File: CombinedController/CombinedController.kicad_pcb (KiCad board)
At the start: 2 copper layers, 2 parts

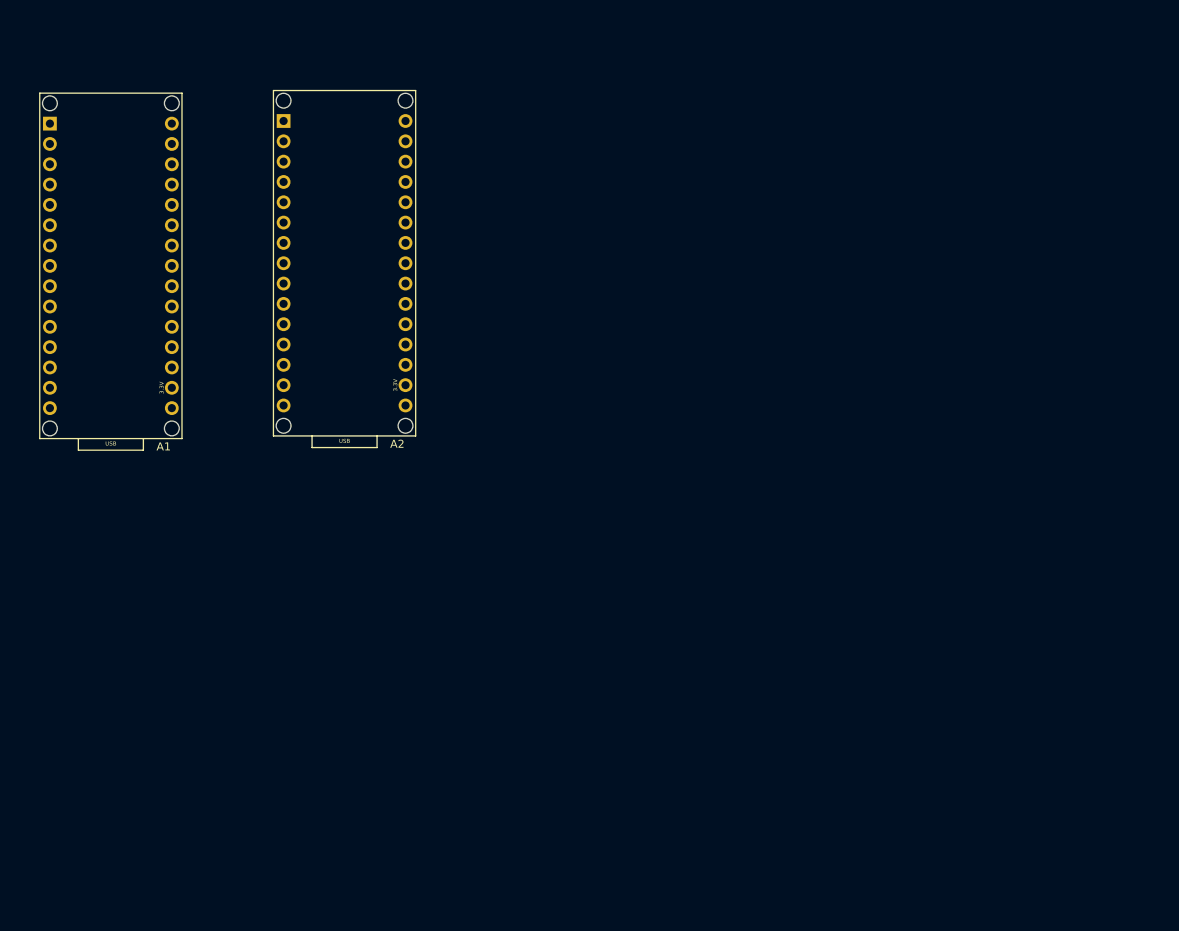
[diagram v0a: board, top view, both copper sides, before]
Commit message: Add MC33886 Footprint and fix schematics
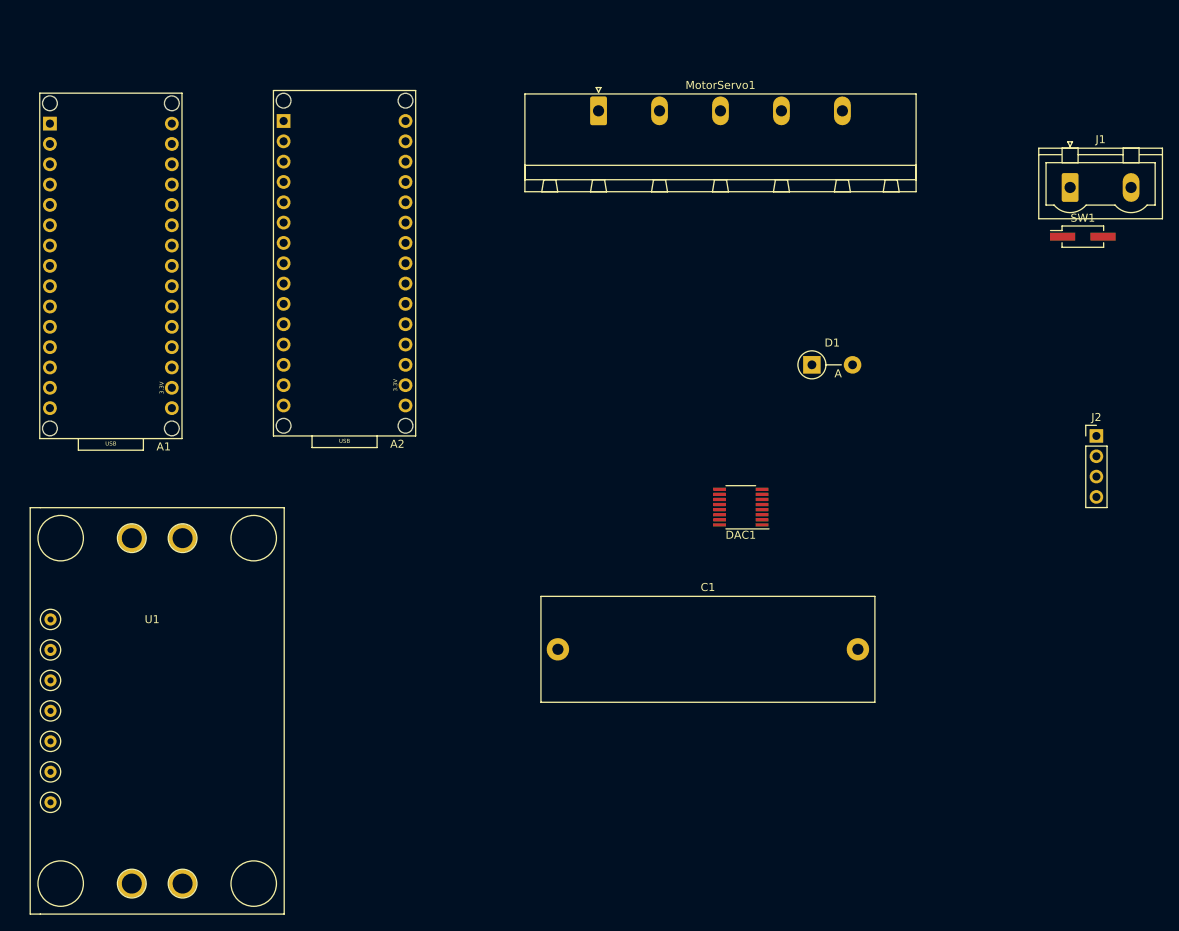
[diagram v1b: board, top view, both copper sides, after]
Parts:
- added C1: C, Capacitor_THT:C_Rect_L41.5mm_W13.0mm_P37.50mm_MKS4, F.Cu at (179.1, 137.2)
- added D1: DIODE, Diode_THT:D_DO-41_SOD81_P5.08mm_Vertical_AnodeUp, F.Cu at (210.8, 101.6)
- added DAC1: MAX5259, Package_SO:QSOP-16_3.9x4.9mm_P0.635mm, F.Cu at (201.9, 119.4)
- added J1: Conn_01x02_Male, Connector_Phoenix_GMSTB:PhoenixContact_GMSTBVA_2,5_2-G-7,62_1x02_P7.62mm_Vertical, F.Cu at (243.1, 79.4)
- added J2: APA102C, Connector_PinHeader_2.54mm:PinHeader_1x04_P2.54mm_Vertical, F.Cu at (246.4, 110.5)
- added MotorServo1: Conn_01x05_Female, Connector_Phoenix_GMSTB:PhoenixContact_GMSTB_2,5_5-GF-7,62_1x05_P7.62mm_Horizontal_ThreadedFlange, F.Cu at (184.2, 69.8)
- added SW1: SW_Push, Connector_PinHeader_2.54mm:PinHeader_2x01_P2.54mm_Vertical_SMD, F.Cu at (244.7, 85.6)
- added U1: MC33886, Arduino:MC33886, F.Cu at (128.3, 132.2)

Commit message: added tle started pcb layouting
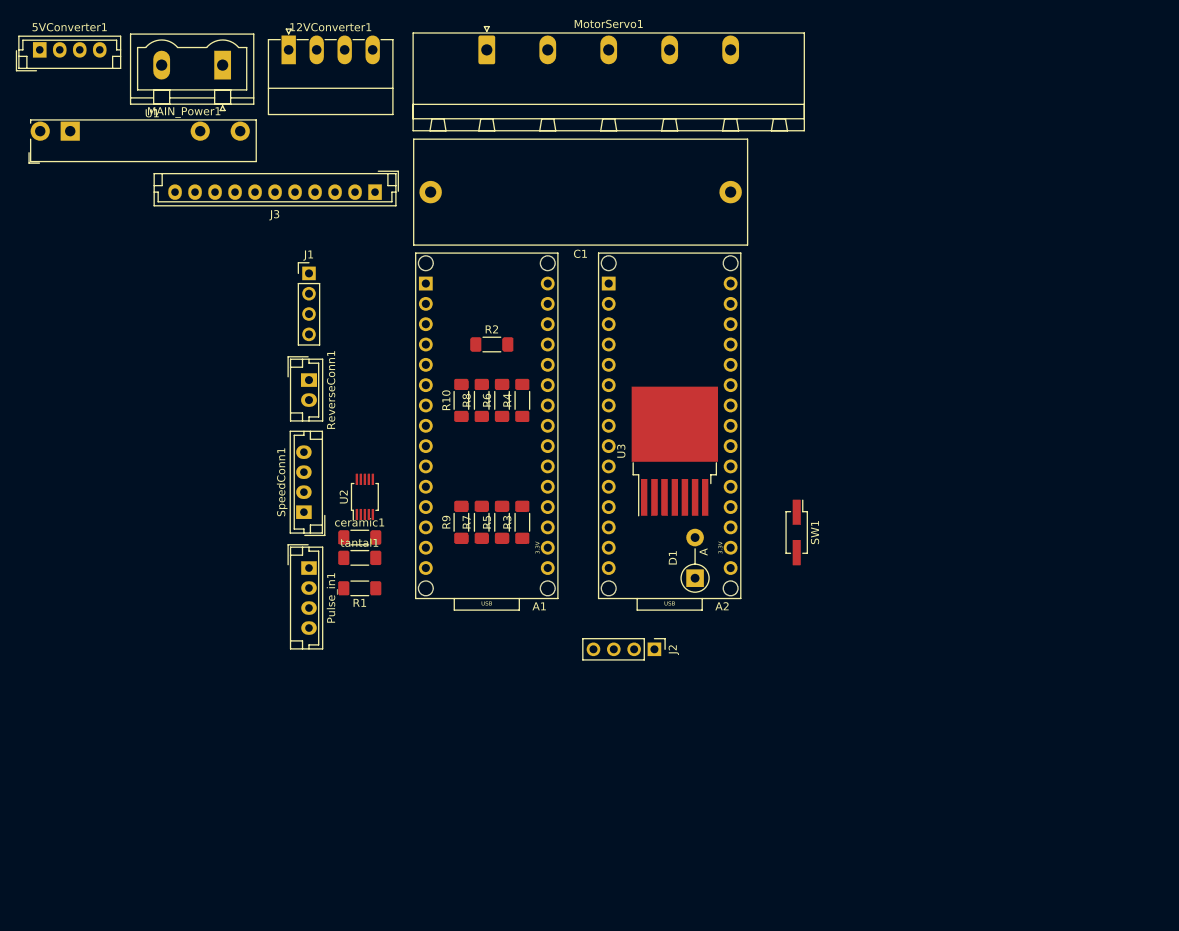
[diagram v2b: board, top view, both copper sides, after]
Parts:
- removed DAC1: MAX5259, Package_SO:QSOP-16_3.9x4.9mm_P0.635mm
- added 12VConverter1: Conn_01x04_Male, Connector_Phoenix_MC:PhoenixContact_MC_1,5_4-G-3.5_1x04_P3.50mm_Horizontal, F.Cu at (145.4, 62.2)
- added 5VConverter1: Conn_01x04_Male, Connector_JST:JST_EH_B04B-EH-A_1x04_P2.50mm_Vertical, F.Cu at (114.3, 62.2)
- added J3: Conn_01x11_Male, Connector_JST:JST_EH_B11B-EH-A_1x11_P2.50mm_Vertical, F.Cu at (156.2, 80.0)
- added MAIN_Power1: Conn_01x02_Male, Connector_Phoenix_GMSTB:PhoenixContact_GMSTBVA_2,5_2-G-7,62_1x02_P7.62mm_Vertical, F.Cu at (137.2, 64.1)
- added Pulse_in1: Conn_01x04_Male, Connector_JST:JST_EH_B04B-EH-A_1x04_P2.50mm_Vertical, F.Cu at (148.0, 127.0)
- added R1: 10kOhm, Resistor_SMD:R_1806_4516Metric, F.Cu at (154.3, 129.5)
- added R10: 1kohm, Resistor_SMD:R_1806_4516Metric, F.Cu at (167.0, 106.0)
- added R2: 10kOhm, Resistor_SMD:R_1806_4516Metric, F.Cu at (170.8, 99.1)
- added R3: R, Resistor_SMD:R_1806_4516Metric, F.Cu at (174.6, 121.3)
- added R4: R, Resistor_SMD:R_1806_4516Metric, F.Cu at (174.6, 106.0)
- added R5: R, Resistor_SMD:R_1806_4516Metric, F.Cu at (172.1, 121.3)
- added R6: R, Resistor_SMD:R_1806_4516Metric, F.Cu at (172.1, 106.0)
- added R7: R, Resistor_SMD:R_1806_4516Metric, F.Cu at (169.5, 121.3)
- added R8: R, Resistor_SMD:R_1806_4516Metric, F.Cu at (169.5, 106.0)
- added R9: 10kohm, Resistor_SMD:R_1806_4516Metric, F.Cu at (167.0, 121.3)
- added ReverseConn1: Conn_01x02_Male, Connector_JST:JST_EH_B02B-EH-A_1x02_P2.50mm_Vertical, F.Cu at (148.0, 103.5)
- added SpeedConn1: Conn_01x04_Male, Connector_JST:JST_EH_B04B-EH-A_1x04_P2.50mm_Vertical, F.Cu at (147.3, 120.0)
- added U2: MCP4728, Package_SO:MSOP-10_3x3mm_P0.5mm, F.Cu at (154.9, 118.1)
- added U3: TLE5205, Package_TO_SOT_SMD:TO-263-7_TabPin4, F.Cu at (193.7, 112.4)
- added ceramic1: 0.1uF, Capacitor_SMD:C_1806_4516Metric, F.Cu at (154.3, 123.2)
- added tantal1: 10uF, Capacitor_SMD:C_1806_4516Metric, F.Cu at (154.3, 125.7)
- J1: value Conn_01x02_Male -> APA102C; footprint Connector_Phoenix_GMSTB:PhoenixContact_GMSTBVA_2,5_2-G-7,62_1x02_P7.62mm_Vertical -> Connector_PinHeader_2.54mm:PinHeader_1x04_P2.54mm_Vertical
- U1: value MC33886 -> 34.81-8240; footprint Arduino:MC33886 -> OptoDevice:Finder_34.81
- moved J1 95.7 mm to (148.0, 90.2)
- moved J2 61.3 mm to (191.1, 137.2), turned to 270 degrees
- moved C1 61.1 mm to (200.7, 80.0), turned to 180 degrees
- moved U1 60.6 mm to (118.1, 72.4)
- moved SW1 51.4 mm to (208.9, 122.6), turned to 270 degrees
- moved A1 51.1 mm to (170.2, 130.8)
- moved A2 45.4 mm to (193.0, 130.8)
- moved D1 30.4 mm to (196.2, 128.3), turned to 90 degrees
- moved MotorServo1 15.9 mm to (170.2, 62.2)
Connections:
- A1 pad 3V3: (no net) -> Net-(A1-Pad3V3)
- A1 pad 5V: (no net) -> 5V_Main
- A1 pad A0: (no net) -> Net-(A1-PadA0)
- A1 pad A1: (no net) -> Net-(A1-PadA1)
- A1 pad A2: (no net) -> Net-(A1-PadA2)
- A1 pad A3: (no net) -> Net-(A1-PadA3)
- A1 pad A4: (no net) -> Net-(A1-PadA4)
- A1 pad A5: (no net) -> Net-(A1-PadA5)
- A1 pad A6: (no net) -> Net-(A1-PadA6)
- A1 pad A7: (no net) -> Net-(A1-PadA7)
- A1 pad AREF: (no net) -> Net-(A1-PadAREF)
- A1 pad D0: (no net) -> Net-(A1-PadD0)
- A1 pad D1: (no net) -> Net-(A1-PadD1)
- A1 pad D10: (no net) -> Net-(A1-PadD10)
- A1 pad D11: (no net) -> Net-(A1-PadD11)
- A1 pad D12: (no net) -> Net-(A1-PadD12)
- A1 pad D13: (no net) -> Net-(A1-PadD13)
- A1 pad D2: (no net) -> Net-(A1-PadD2)
- A1 pad D3: (no net) -> Net-(A1-PadD3)
- A1 pad D4: (no net) -> Mode
- A1 pad D5: (no net) -> Lenkung
- A1 pad D6: (no net) -> Throttle
- A1 pad D7: (no net) -> Net-(A1-PadD7)
- A1 pad D8: (no net) -> Net-(A1-PadD8)
- A1 pad D9: (no net) -> Net-(A1-PadD9)
- A1 pad GND1: (no net) -> GND
- A1 pad GND2: (no net) -> GND
- A1 pad RST1: (no net) -> Net-(A1-PadRST1)
- A1 pad RST2: (no net) -> Net-(A1-PadRST2)
- A1 pad VIN: (no net) -> Net-(A1-PadVIN)
- A2 pad 3V3: (no net) -> Net-(A2-Pad3V3)
- A2 pad 5V: (no net) -> 5V_2
- A2 pad A0: (no net) -> Net-(A2-PadA0)
- A2 pad A1: (no net) -> Net-(A2-PadA1)
- A2 pad A2: (no net) -> Net-(A2-PadA2)
- A2 pad A3: (no net) -> Net-(A2-PadA3)
- A2 pad A4: (no net) -> Net-(A2-PadA4)
- A2 pad A5: (no net) -> Net-(A2-PadA5)
- A2 pad A6: (no net) -> Net-(A2-PadA6)
- A2 pad A7: (no net) -> Net-(A2-PadA7)
- A2 pad AREF: (no net) -> Net-(A2-PadAREF)
- A2 pad D0: (no net) -> Net-(A2-PadD0)
- A2 pad D1: (no net) -> Net-(A2-PadD1)
- A2 pad D10: (no net) -> Net-(A2-PadD10)
- A2 pad D11: (no net) -> Net-(A2-PadD11)
- A2 pad D12: (no net) -> Lenkung
- A2 pad D13: (no net) -> Net-(A2-PadD13)
- A2 pad D2: (no net) -> Net-(A2-PadD2)
- A2 pad D3: (no net) -> Net-(A2-PadD3)
- A2 pad D4: (no net) -> Net-(A2-PadD4)
- A2 pad D5: (no net) -> Net-(A2-PadD5)
- A2 pad D6: (no net) -> Net-(A2-PadD6)
- A2 pad D7: (no net) -> Net-(A2-PadD7)
- A2 pad D8: (no net) -> Net-(A2-PadD8)
- A2 pad D9: (no net) -> Net-(A2-PadD9)
- A2 pad GND1: (no net) -> GND
- A2 pad GND2: (no net) -> GND
- A2 pad RST1: (no net) -> Net-(A2-PadRST1)
- A2 pad RST2: (no net) -> Net-(A2-PadRST2)
- A2 pad VIN: (no net) -> 12V
- C1 pad 1: Net-(A2-Pad19) -> Net-(A2-PadA0)
- J1 pad 1: 12V -> GND
- J1 pad 2: GND -> Net-(A1-PadD2)
- J2 pad 2: Net-(A2-Pad7) -> Net-(A2-PadD4)
- J2 pad 3: Net-(A2-Pad8) -> Net-(A2-PadD5)
- MotorServo1 pad 3: Net-(A2-Pad19) -> Net-(A2-PadA0)
- SW1 pad 2: Net-(A2-Pad16) -> Net-(A2-PadD13)

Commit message: pcb initial
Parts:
- removed J2: APA102C, Connector_PinHeader_2.54mm:PinHeader_1x04_P2.54mm_Vertical
- removed R1, R2: 10kOhm, Resistor_SMD:R_1806_4516Metric
- added Q1: BSS138, Package_TO_SOT_SMD:SOT-23, F.Cu at (223.5, 109.2)
- added Q2: BSS138, Package_TO_SOT_SMD:SOT-23, F.Cu at (223.5, 118.1)
- added R11: R, Resistor_THT:R_Axial_DIN0207_L6.3mm_D2.5mm_P7.62mm_Horizontal, F.Cu at (212.1, 108.0)
- added R12: R, Resistor_THT:R_Axial_DIN0207_L6.3mm_D2.5mm_P7.62mm_Horizontal, F.Cu at (212.1, 116.8)
- added R13: R, Resistor_THT:R_Axial_DIN0207_L6.3mm_D2.5mm_P7.62mm_Horizontal, F.Cu at (218.4, 113.0)
- added R14: R, Resistor_THT:R_Axial_DIN0207_L6.3mm_D2.5mm_P7.62mm_Horizontal, F.Cu at (218.4, 121.9)
- added U4: NodeMCU_Amica_R2, nodemcu:NodeMCU_Amica_R2, F.Cu at (205.7, 90.2)
- added U5: SK9822, TLE5205:APA102_hand_solder, F.Cu at (171.4, 130.8)
- added U6: SK9822, TLE5205:APA102_hand_solder, F.Cu at (190.5, 130.8)
- 12VConverter1: value Conn_01x04_Male -> Conn_01x03_Male; footprint Connector_Phoenix_MC:PhoenixContact_MC_1,5_4-G-3.5_1x04_P3.50mm_Horizontal -> Connector_Phoenix_MSTB:PhoenixContact_MSTBVA_2,5_3-G_1x03_P5.00mm_Vertical
- 5VConverter1: footprint Connector_JST:JST_EH_B04B-EH-A_1x04_P2.50mm_Vertical -> Connector_Phoenix_MSTB:PhoenixContact_MSTBVA_2,5_3-G_1x03_P5.00mm_Vertical
- A1, A2: footprint Arduino:Arduino_Nano_Socket -> Module:Arduino_Nano_WithMountingHoles
- C1: footprint Capacitor_THT:C_Rect_L41.5mm_W13.0mm_P37.50mm_MKS4 -> Capacitor_THT:CP_Radial_Tantal_D8.0mm_P5.00mm
- J1: value APA102C -> PWR_C; footprint Connector_PinHeader_2.54mm:PinHeader_1x04_P2.54mm_Vertical -> Connector_JST:JST_EH_B02B-EH-A_1x02_P2.50mm_Vertical
- MotorServo1: footprint Connector_Phoenix_GMSTB:PhoenixContact_GMSTB_2,5_5-GF-7,62_1x05_P7.62mm_Horizontal_ThreadedFlange -> Connector_Phoenix_MSTB:PhoenixContact_MSTBVA_2,5_5-G-5,08_1x05_P5.08mm_Vertical
- R10, R3, R4, R5, R6, R7, R8, R9: footprint Resistor_SMD:R_1806_4516Metric -> Resistor_SMD:R_0805_2012Metric_Pad1.15x1.40mm_HandSolder; moved to B.Cu
- U2, U3, ceramic1, tantal1: moved to B.Cu
- moved J3 85.1 mm to (233.7, 115.3), turned to 90 degrees
- moved 5VConverter1 83.9 mm to (196.8, 77.5), turned to 180 degrees
- moved MotorServo1 57.9 mm to (226.1, 77.5), turned to 180 degrees
- moved D1 54.0 mm to (228.6, 85.1), turned to 180 degrees
- moved U1 53.0 mm to (154.9, 110.5), turned to 90 degrees
- moved A2 40.7 mm to (182.9, 91.4)
- moved A1 40.4 mm to (161.3, 91.4)
- moved 12VConverter1 35.8 mm to (177.8, 77.5), turned to 180 degrees
- moved C1 34.4 mm to (234.9, 77.5), turned to 270 degrees
- moved R3 31.4 mm to (152.4, 99.1), turned to 0 degrees
- moved U3 28.4 mm to (217.2, 96.5), turned to 270 degrees
- moved R5 27.8 mm to (152.4, 101.6), turned to 0 degrees
- moved MAIN_Power1 25.4 mm to (158.8, 77.5)
- moved R7 24.2 mm to (152.4, 104.1), turned to 0 degrees
- moved R9 20.7 mm to (152.4, 106.7), turned to 0 degrees
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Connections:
- 5VConverter1 pad 3: GND -> Net-(12VConverter1-Pad3)
- C1 pad 1: Net-(A2-PadA0) -> SERVO_In
- J1 pad 1: GND -> Net-(J1-Pad1)
- J1 pad 2: Net-(A1-PadD2) -> (no net)
- J3 pad 3: Lenkung -> Net-(J3-Pad3)
- J3 pad 4: Throttle -> Net-(J3-Pad4)
- J3 pad 5: Mode -> Net-(J3-Pad5)
- MAIN_Power1 pad 1: Net-(12VConverter1-Pad4) -> Net-(12VConverter1-Pad3)
- MotorServo1 pad 3: Net-(A2-PadA0) -> SERVO_In
- R10 pad 1: Net-(A1-PadA3) -> P_IN_D
- R3 pad 2: Net-(A1-PadA0) -> P_IN_A
- R4 pad 1: Net-(A1-PadA0) -> P_IN_A
- R5 pad 2: Net-(A1-PadA1) -> P_IN_B
- R6 pad 1: Net-(A1-PadA1) -> P_IN_B
- R7 pad 2: Net-(A1-PadA2) -> P_IN_C
- R8 pad 1: Net-(A1-PadA2) -> P_IN_C
- R9 pad 2: Net-(A1-PadA3) -> P_IN_D
- ReverseConn1 pad 1: Net-(A1-PadD9) -> Net-(A1-Pad12)
- ReverseConn1 pad 2: Net-(A1-PadD10) -> Net-(A1-Pad13)
- SW1 pad 2: Net-(A2-PadD13) -> Net-(A2-Pad16)
- SpeedConn1 pad 1: Net-(A1-PadA7) -> VOUTD
- SpeedConn1 pad 2: Net-(A1-PadA6) -> VOUTC
- SpeedConn1 pad 3: Net-(A1-PadA5) -> VOUTB
- SpeedConn1 pad 4: Net-(A1-PadA4) -> VOUTA
- U1 pad 11: Net-(12VConverter1-Pad4) -> Net-(J1-Pad1)
- U1 pad A2: Net-(A1-PadD7) -> Power_Relay
- U2 pad 2: Net-(A1-PadD12) -> SCL_DA
- U2 pad 3: Net-(A1-PadD11) -> SDA_DA
- U2 pad 4: GND -> Net-(U2-Pad4)
- U2 pad 6: Net-(A1-PadA4) -> VOUTA
- U2 pad 7: Net-(A1-PadA5) -> VOUTB
- U2 pad 8: Net-(A1-PadA6) -> VOUTC
- U2 pad 9: Net-(A1-PadA7) -> VOUTD
- U3 pad 2: Net-(A2-PadD11) -> EF
- U3 pad 3: Net-(A2-PadD10) -> IN1
- U3 pad 5: Net-(A2-PadD8) -> IN2
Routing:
- net GND: track 0.00 -> 357.7 mm, vias 0 -> 3
- net 5V_Main: track 0.00 -> 233.7 mm, vias 0 -> 3
- net SCL_H: track 0.00 -> 130.4 mm
- net SDA_H: track 0.00 -> 104.2 mm
- net 12V: track 0.00 -> 103.2 mm, vias 0 -> 1
- net SERVO_In: track 0.00 -> 96.4 mm, vias 0 -> 1
- net VOUTD: track 0.00 -> 59.2 mm
- net VOUTC: track 0.00 -> 56.0 mm
- net IN2: track 0.00 -> 52.0 mm, vias 0 -> 1
- net VOUTB: track 0.00 -> 49.7 mm
- net IN1: track 0.00 -> 49.5 mm, vias 0 -> 2
- net VOUTA: track 0.00 -> 49.5 mm
- net EF: track 0.00 -> 49.3 mm, vias 0 -> 1
- net Net-(12VConverter1-Pad3): track 0.00 -> 45.5 mm
- net 5V_2: track 0.00 -> 41.8 mm
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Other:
- board outline added: 94 x 66 mm
- net class Default: trace_width 0.25 -> 1
- net class small added: clearance 0.2, trace_width 0.5, via_dia 0.8, via_drill 0.4

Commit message: initial cnc working
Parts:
- added Main_Light1: Conn_01x02_Male, Connector_Phoenix_MSTB:PhoenixContact_MSTBVA_2,5_4-G_1x04_P5.00mm_Vertical, F.Cu at (236.2, 129.5)
- A1, A2: footprint Module:Arduino_Nano_WithMountingHoles -> Arduino:Arduino_Nano_Socket
- D1: moved to B.Cu
- J3: footprint Connector_JST:JST_EH_B11B-EH-A_1x11_P2.50mm_Vertical -> Connector_JST:JST_EH_B07B-EH-A_1x07_P2.50mm_Vertical
- ceramic1, tantal1: footprint Capacitor_SMD:C_1806_4516Metric -> Capacitor_SMD:C_0402_1005Metric
- moved A1 40.1 mm to (169.1, 130.8)
- moved A2 40.1 mm to (190.5, 130.8)
- moved tantal1 11.4 mm to (156.2, 120.7)
- moved J3 9.88 mm to (234.3, 105.4)
- moved ceramic1 6.35 mm to (156.2, 121.9)
- moved D1 0.64 mm to (228.6, 84.5)
- moved U3 0.64 mm to (217.2, 97.2)
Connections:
- J3 pad 2: 5V_Main -> Net-(J3-Pad2)
- J3 pad 4: Net-(J3-Pad4) -> 5V_Main
- ReverseConn1 pad 1: Net-(A1-Pad12) -> Net-(A1-PadD9)
- ReverseConn1 pad 2: Net-(A1-Pad13) -> Net-(A1-PadD10)
- SW1 pad 2: Net-(A2-Pad16) -> Net-(A2-PadD13)
- U4 pad 22: Net-(J3-Pad5) -> Net-(Main_Light1-Pad2)
- U4 pad 23: Net-(J3-Pad6) -> Net-(Main_Light1-Pad3)
- U4 pad 26: Net-(J3-Pad7) -> Net-(J3-Pad2)
- U4 pad 27: Net-(J3-Pad8) -> Net-(J3-Pad3)
- U4 pad 28: Net-(J3-Pad9) -> Net-(J3-Pad5)
- U4 pad 29: Net-(J3-Pad10) -> Net-(J3-Pad6)
- U4 pad 30: Net-(J3-Pad11) -> Net-(J3-Pad7)
- U5 pad 1: Net-(A1-Pad6) -> Net-(A1-PadD3)
- U5 pad 2: Net-(A1-Pad5) -> Net-(A1-PadD2)
- U6 pad 1: Net-(A2-Pad8) -> Net-(A2-PadD5)
- U6 pad 2: Net-(A2-Pad9) -> Net-(A2-PadD6)
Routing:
- net 5V_Main: track 233.7 -> 288.5 mm, vias 3 -> 4
- net Net-(A1-PadD2): track 0.00 -> 39.8 mm, vias 0 -> 2
- net Net-(A1-Pad5): track 39.8 -> 0.00 mm, vias 2 -> 0
- net Net-(A1-PadD3): track 0.00 -> 33.8 mm, vias 0 -> 2
- net Net-(A1-Pad6): track 33.8 -> 0.00 mm, vias 2 -> 0
- net Net-(A2-PadD5): track 0.00 -> 22.8 mm
- net Net-(A2-Pad8): track 22.8 -> 0.00 mm
- net Net-(A2-PadD6): track 0.00 -> 22.6 mm
- net Net-(A2-Pad9): track 22.6 -> 0.00 mm
- net Net-(Main_Light1-Pad2): track 0.00 -> 18.9 mm
- net Net-(Main_Light1-Pad3): track 0.00 -> 17.2 mm
- net Net-(A1-PadD10): track 0.00 -> 13.6 mm
- net Net-(A1-Pad13): track 13.6 -> 0.00 mm
- net Net-(A1-PadD9): track 0.00 -> 13.5 mm
- net Net-(A1-Pad12): track 13.5 -> 0.00 mm
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- added copper zone on B.Cu, net GND
- added copper zone on F.Cu, net GND
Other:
- net class Default: trace_width 1 -> 0.25
